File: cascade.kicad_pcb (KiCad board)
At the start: 2 copper layers, 91 x 59 mm, 16 parts, among them J1 Conn_01x01, J2 Conn_01x01, J3 Conn_01x01, J4 Conn_01x01

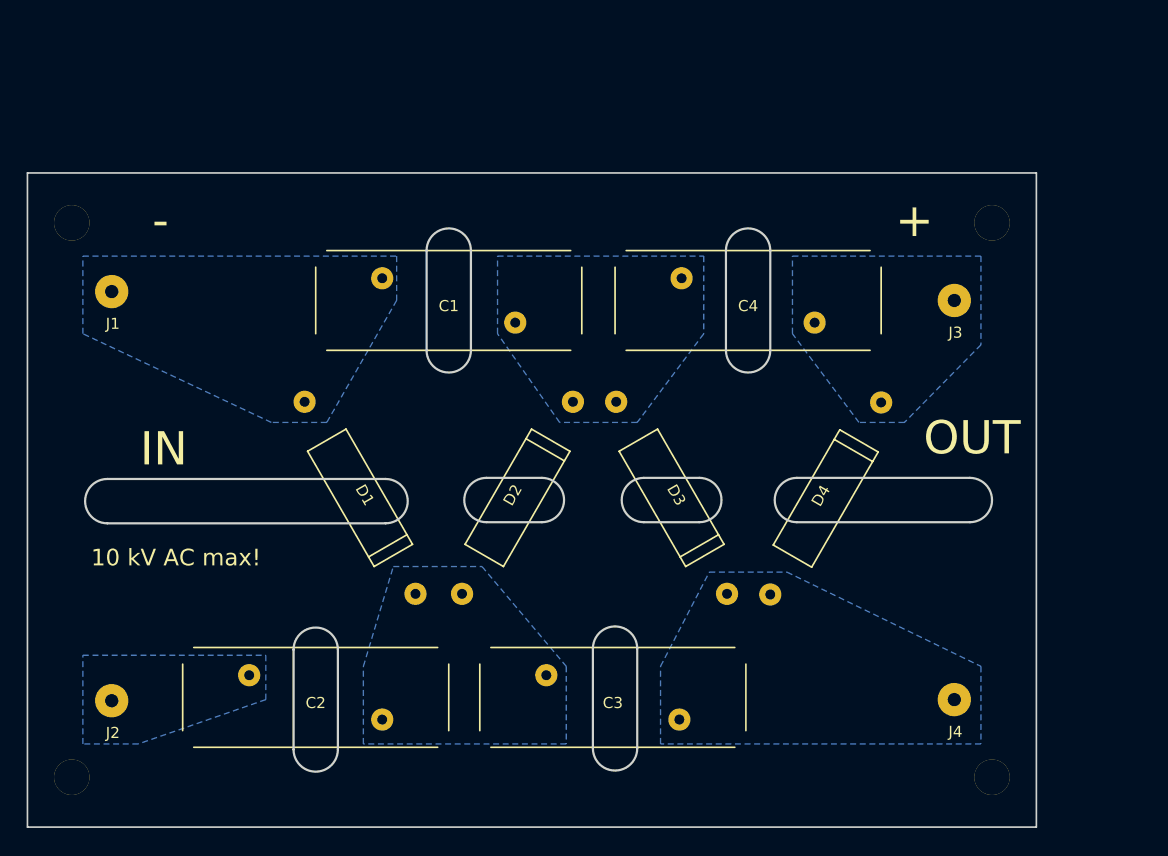
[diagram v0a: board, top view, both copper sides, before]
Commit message: Move to new high density design
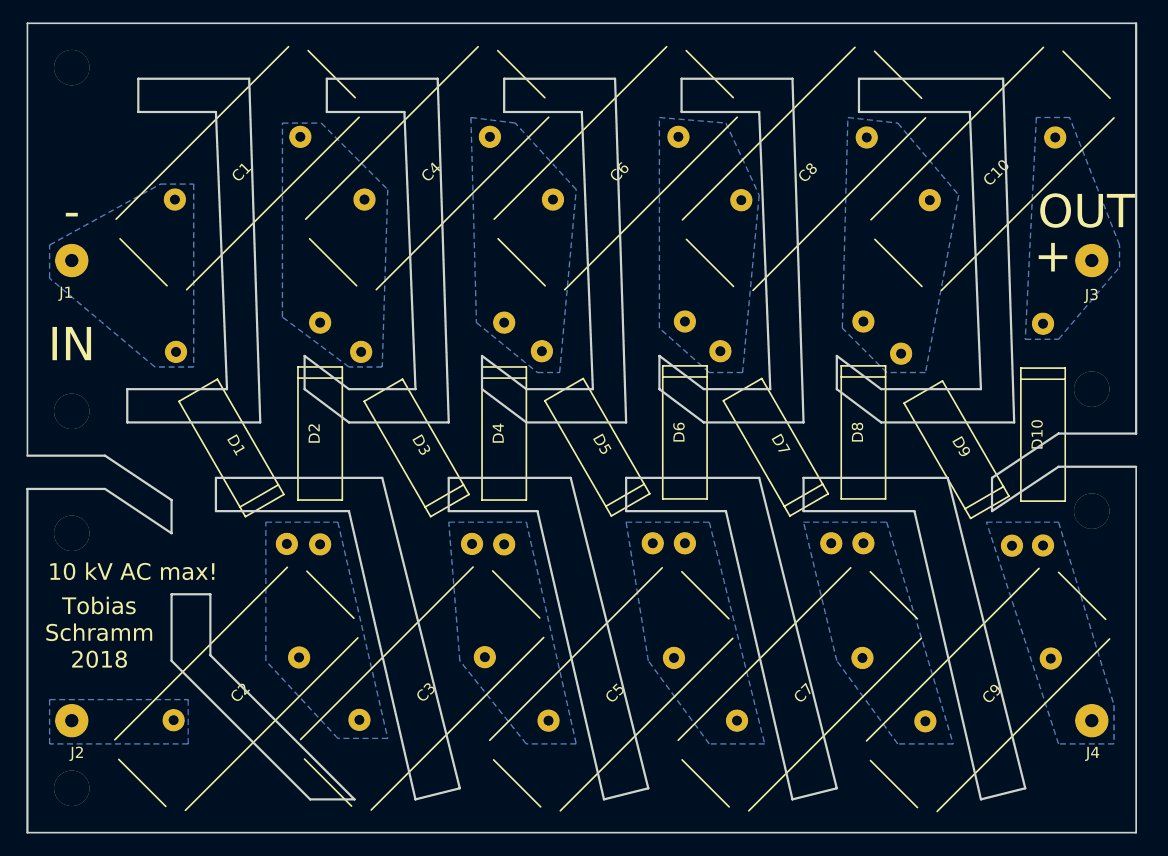
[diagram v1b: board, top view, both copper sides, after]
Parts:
- added C10: C, cascade:cap_20kv_10nf, F.Cu at (119.0, 48.1)
- added C5: C, cascade:cap_20kv_10nf, F.Cu at (84.7, 95.1)
- added C6: C, cascade:cap_20kv_10nf, F.Cu at (85.1, 48.1)
- added C7: C, cascade:cap_20kv_10nf, F.Cu at (101.7, 95.1)
- added C8: C, cascade:cap_20kv_10nf, F.Cu at (102.0, 48.1)
- added C9: C, cascade:cap_20kv_10nf, F.Cu at (118.6, 95.1)
- added D10: D, cascade:diode_2CL2FM, F.Cu at (123.6, 72.1)
- added D5: D, cascade:diode_2CL2FM, F.Cu at (83.4, 73.2)
- added D6: D, cascade:diode_2CL2FM, F.Cu at (91.3, 71.9)
- added D7: D, cascade:diode_2CL2FM, F.Cu at (99.5, 73.2)
- added D8: D, cascade:diode_2CL2FM, F.Cu at (107.4, 71.9)
- added D9: D, cascade:diode_2CL2FM, F.Cu at (115.8, 73.5)
- added REF**: mounthole, cascade:mounthole, F.Cu at (36.0, 70.0)
- added REF**: mounthole, cascade:mounthole, F.Cu at (36.0, 81.0)
- moved C4 31.3 mm to (68.1, 48.1), turned to 45 degrees
- moved D4 29.6 mm to (75.0, 72.0), turned to 270 degrees
- moved REF** 25.6 mm to (128.0, 79.0)
- moved D3 23.4 mm to (67.1, 73.3)
- moved C1 22.5 mm to (51.0, 48.1), turned to 45 degrees
- moved D2 18.7 mm to (58.4, 72.0), turned to 270 degrees
- moved REF** 17.5 mm to (128.0, 68.0)
- moved C3 17.2 mm to (67.6, 95.0), turned to 45 degrees
- moved REF** 14.0 mm to (36.0, 39.0)
- moved J3 12.9 mm to (128.0, 56.4)
- moved J4 12.5 mm to (128.0, 97.9)
- moved D1 12.4 mm to (50.4, 73.3)
- moved C2 7.20 mm to (50.8, 95.0), turned to 45 degrees
- moved J1 5.05 mm to (35.4, 56.4)
- moved J2 3.67 mm to (36.4, 97.9)
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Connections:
- J3 pad 1: Net-(C4-Pad2) -> Net-(C10-Pad2)
- J4 pad 1: Net-(C3-Pad2) -> Net-(C9-Pad2)
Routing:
- added copper zone on B.Cu, net Net-(C10-Pad1)
- added copper zone on B.Cu, net Net-(C10-Pad2)
- added copper zone on B.Cu, net Net-(C5-Pad2)
- added copper zone on B.Cu, net Net-(C6-Pad2)
- added copper zone on B.Cu, net Net-(C7-Pad2)
- added copper zone on B.Cu, net Net-(C9-Pad2)
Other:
- board size 91 x 59 mm -> 100 x 73 mm
- board text added: "Tobias Schramm 2018"
